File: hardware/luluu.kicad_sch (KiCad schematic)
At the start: 56 parts, among them J1 BATT_CON, J2 RPi SWD, J3 STEMMA_{QT} I_{2}C, J4 Micro_SD_Card, J5 RPi UART, J6 USB_C_Receptacle_USB2.0, J7 DISP_LCD_ST7789, Q1 AO3401A, Q2 BSS138, SW1 SW_USBBOOT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

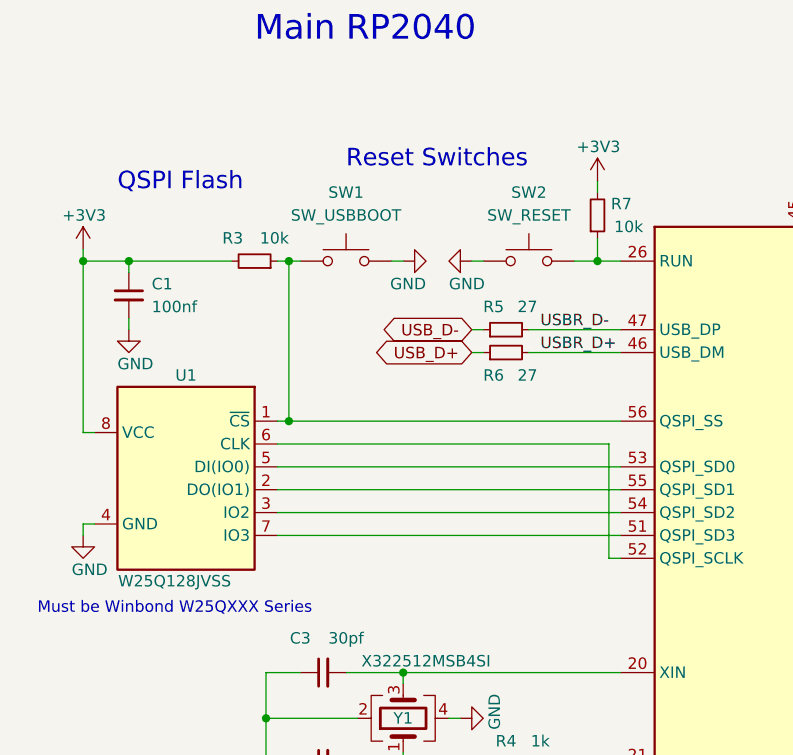
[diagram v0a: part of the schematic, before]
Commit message: rev1.1 - fix USB data and 1k boot resistor
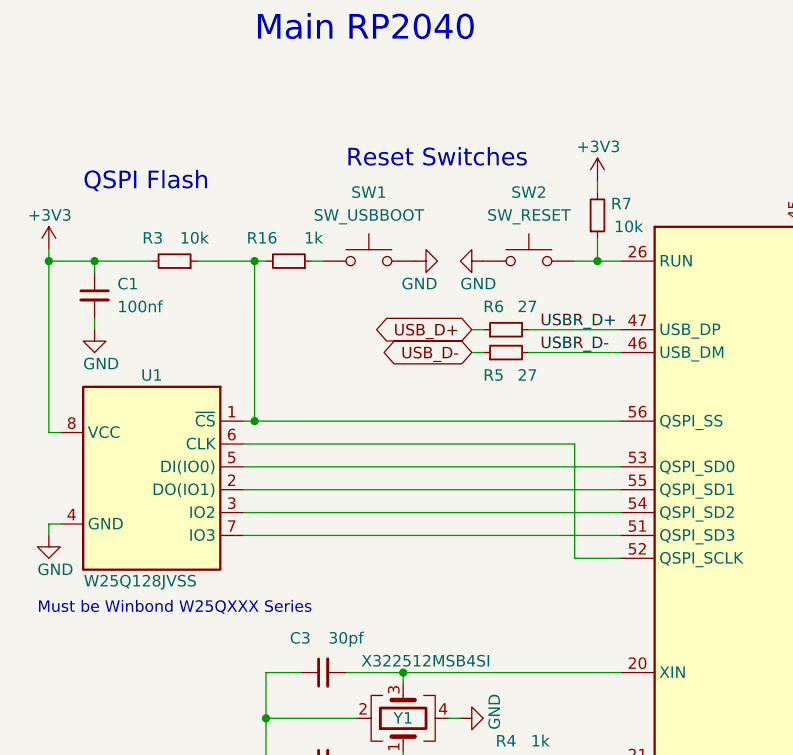
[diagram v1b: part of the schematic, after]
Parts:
- added R16: 1k, Resistor_SMD:R_0603_1608Metric_Pad0.98x0.95mm_HandSolder, symbol Device:R_Small
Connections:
- net USBR_D+: now also U3.47 (USB_DP); no longer U3.46 (USB_DM)
- net USBR_D-: now also U3.46 (USB_DM); no longer U3.47 (USB_DP)
- net at R3.1, U1.1 (~{CS}), U3.56 (QSPI_SS): now also R16.2; no longer SW1.1
- new net: R16.1, SW1.1
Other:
- moved on the sheet: C1, R3, R5, R6, SW1, U1

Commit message: start on rev2 of pcb
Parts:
- removed J5: RPi UART, Connector_JST:JST_SH_BM03B-SRSS-TB_1x03-1MP_P1.00mm_Vertical, symbol Connector_Generic:Conn_01x03
- removed U5: APX803S-26/29, Package_TO_SOT_SMD:SOT-23-3, symbol luluu:APX803S-26SA
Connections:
- net UART_{RX} is gone; now on net CARD_~{CS}: U3.3 (GPIO1)
- net +3V3: now also SW3.2 (B); no longer C5.1, C6.1, U2.5 (VOUT)
- net +BATT: now also J1.1 (Pin_1); no longer SW3.2 (B)
- net I_{2}C_{CLOCK}: now also U3.14 (GPIO11); no longer U3.5 (GPIO3)
- net I_{2}C_{DATA}: now also U3.13 (GPIO10); no longer U3.4 (GPIO2)
- net at SW3.1 (A): now also C5.1, C6.1, U2.5 (VOUT); no longer J1.1 (Pin_1)
- net CARD_SPI_{MISO}: now reaches U3.6 (GPIO4)
- net CARD_SPI_{MISO}: now also J4.7 (DAT0)
- net CARD ~{CS} renamed CARD_~{CS}
- net CARD_~{CS}: no longer U3.7 (GPIO5)
- net DISP BACKLIGHT renamed DISP_BACKLIGHT
- net DISP CS_{DATA/~{CMD}} renamed DISP_CS_{DATA/~{CMD}}
- net DISP VSYNC renamed DISP_VSYNC
- net DISP ~{CS_{MAIN}} renamed DISP_~{CS_{MAIN}}
- net DISP ~{RESET} renamed DISP_~{RESET}
- net SPI_{CLOCK} renamed DISP_SPI_{CLOCK}
- net DISP_SPI_{CLOCK}: no longer J4.5 (CLK)
- net SPI_{MISO}: no longer names the net of U3.11 (GPIO8)
- net SPI_{MISO}: no longer J4.7 (DAT0)
- net SPI_{MOSI} renamed DISP_SPI_{MOSI}
- net DISP_SPI_{MOSI}: no longer J4.3 (CMD)
- net UART_{TX}: no longer names the net of U3.2 (GPIO0)
- new net CARD_SPI_{CLOCK}: J4.5 (CLK), U3.4 (GPIO2)
- new net CARD_SPI_{MOSI}: J4.3 (CMD), U3.5 (GPIO3)
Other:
- note removed: "UART & I_{2}C compatible with Adafruit Feather GPIO Layout"
- moved on the sheet: J2, SW3

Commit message: pcb rev 2.0 progress
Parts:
- added D2: CHRG, LED_SMD:LED_0805_2012Metric_Pad1.15x1.40mm_HandSolder, symbol Device:LED
- added R17: 1k, Resistor_SMD:R_0603_1608Metric_Pad0.98x0.95mm_HandSolder, symbol Device:R_Small
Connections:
- net +5V: now also R17.2
- net CARD_SPI_{MISO}: now also U3.2 (GPIO0); no longer U3.6 (GPIO4)
- net CARD_~{CS}: now also U3.7 (GPIO5); no longer U3.3 (GPIO1)
- net at U4.1 (~{CHRG}): now also D2.1 (K)
- new net: D2.2 (A), R17.1
- no-connect marks 24 -> 23
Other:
- moved on the sheet: C7

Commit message: more work on v2.0
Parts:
- added J5: GPIO0, Connector_PinHeader_2.54mm:PinHeader_1x05_P2.54mm_Vertical, symbol Connector_Generic:Conn_01x05
- added J8: GPIO1, Connector_PinHeader_2.54mm:PinHeader_1x07_P2.54mm_Vertical, symbol Connector_Generic:Conn_01x07
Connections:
- net +3V3: now also J8.6 (Pin_6)
- net GND: now also J5.1 (Pin_1), J8.7 (Pin_7)
- net GPIO_D8: now reaches U3.11 (GPIO8)
- net GPIO_D8: now also J5.3 (Pin_3)
- net GPIO_D9: now reaches U3.12 (GPIO9)
- net GPIO_D9: now also J5.4 (Pin_4)
- net GPIO_D12: now reaches U3.15 (GPIO12)
- net GPIO_D12: now also J5.5 (Pin_5)
- net GPIO_D24: now reaches U3.36 (GPIO24)
- net GPIO_D24: now also J8.5 (Pin_5)
- net GPIO_D25: now reaches U3.37 (GPIO25)
- net GPIO_D25: now also J8.4 (Pin_4)
- net GPIO_A0: now reaches U3.38 (GPIO26_ADC0)
- net GPIO_A0: now also J8.3 (Pin_3)
- net GPIO_A1: now reaches U3.39 (GPIO27_ADC1)
- net GPIO_A1: now also J8.2 (Pin_2)
- net GPIO_A2: now reaches U3.40 (GPIO28_ADC2)
- net GPIO_A2: now also J8.1 (Pin_1)
- net GPIO_D7: now reaches U3.9 (GPIO7)
- net GPIO_D7: now also J5.2 (Pin_2)
- no-connect marks 23 -> 14

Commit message: more work on v2
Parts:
- added H1, H2, H3, H4, H5: MH, luluu:MountingHole_1.1mm_M1, symbol Mechanical:MountingHole
- added JP1: SW_A_JMPER, Jumper:SolderJumper-3_P1.3mm_Bridged12_RoundedPad1.0x1.5mm, symbol Jumper:SolderJumper_3_Bridged12
- added JP2: SW_B_JMPER, Jumper:SolderJumper-3_P1.3mm_Bridged12_RoundedPad1.0x1.5mm, symbol Jumper:SolderJumper_3_Bridged12
- SW1: value SW_USBBOOT -> SW_B
- SW2: value SW_RESET -> SW_A
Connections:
- net SW_A_RST: now reaches R7.1, U3.26 (RUN)
- net SW_A_RST: now also JP1.1 (A); no longer SW2.2
- net SW_A_GPIO: now reaches U3.3 (GPIO1)
- net SW_A_GPIO: now also JP1.3 (B)
- net SW_B_GPIO: now reaches U3.8 (GPIO6)
- net SW_B_GPIO: now also JP2.3 (B)
- net at SW1.1: now also JP2.2 (C); no longer R16.1
- new net: JP1.2 (C), SW2.2
- new net SW_B_BOOT: JP2.1 (A), R16.1
- no-connect marks 14 -> 12
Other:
- note added: "Mount Holes"
- note added: "Pin Headers"
- note added: "Push Switches"
- note removed: "Reset Switches"
- moved on the sheet: C1, C10, C11, C12, C13, C14, C15, C16, C17, C18, C19, C3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

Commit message: 2.0 release candidate
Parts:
- removed C21: 100nf, Capacitor_SMD:C_0402_1005Metric_Pad0.74x0.62mm_HandSolder, symbol Device:C_Small
- added C23: 100nf, Capacitor_SMD:C_0402_1005Metric_Pad0.74x0.62mm_HandSolder, symbol Device:C_Small
- added JP3: Accel Addr LSB, Jumper:SolderJumper-2_P1.3mm_Open_RoundedPad1.0x1.5mm, symbol Jumper:SolderJumper_2_Open
- added R18, R19: 5.1k, Resistor_SMD:R_0603_1608Metric_Pad0.98x0.95mm_HandSolder, symbol Device:R_Small
- added R20: 10k, Resistor_SMD:R_0603_1608Metric_Pad0.98x0.95mm_HandSolder, symbol Device:R_Small
- added U5: LIS3DH, Package_LGA:LGA-16_3x3mm_P0.5mm_LayoutBorder3x5y, symbol Sensor_Motion:LIS3DH
- H1, H2, H3: footprint luluu:MountingHole_1.1mm_M1 -> luluu:MountingHole_1.3mm_M1.2_Pad; now left out of the parts list
- H4, H5: footprint luluu:MountingHole_1.1mm_M1 -> luluu:MountingHole_1.3mm_M1.2; now left out of the parts list
- J5: footprint Connector_PinHeader_2.54mm:PinHeader_1x05_P2.54mm_Vertical -> luluu:PinHeader_1x06_P2.54mm_Vertical; symbol Connector_Generic:Conn_01x05 -> Connector_Generic:Conn_01x06; now left out of the parts list
- J7: footprint luluu:FPC_24_SOLDER -> luluu:FPC_24_JUSHUO_AFC04-S24XCA-00; LCSC (none) -> C883644; now in the parts list
- J8: footprint Connector_PinHeader_2.54mm:PinHeader_1x07_P2.54mm_Vertical -> luluu:PinHeader_1x07_P2.54mm_Vertical; now left out of the parts list
- JP1, JP2: now left out of the parts list
- R17: value 1k -> 10k
- R9: value 5.1k -> 10k
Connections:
- net +3V3: now also J8.7 (Pin_7), R3.1, R7.1, C23.1, JP3.1 (A), R18.1, R19.1, U5.1 (VDD_IO), U5.14 (VDD), U5.8 (CS); no longer J8.6 (Pin_6), R3.2, R7.2, R9.2
- net +BATT: now also J5.1 (Pin_1)
- net CARD_~{CS}: now also U3.6 (GPIO4); no longer U3.7 (GPIO5)
- net DISP_BACKLIGHT: now also R9.2, U3.13 (GPIO10); no longer R9.1, U3.34 (GPIO22)
- net DISP_CS_{DATA/~{CMD}}: now also U3.16 (GPIO13); no longer U3.29 (GPIO18)
- net DISP_~{CS_{MAIN}}: now also U3.15 (GPIO12); no longer U3.30 (GPIO19)
- net DISP_~{RESET}: now also U3.14 (GPIO11); no longer U3.28 (GPIO17)
- net GND: now also J5.2 (Pin_2), J8.6 (Pin_6), R9.1, C23.2, R20.1, U5.10 (GND), U5.12 (GND), U5.13 (ADC3), U5.15 (ADC2), U5.16 (ADC1), U5.5 (GND); no longer J5.1 (Pin_1), J8.7 (Pin_7)
- net GPIO_D24: now also U5.11 (INT1)
- net GPIO_D7: now also J5.4 (Pin_4); no longer J5.2 (Pin_2)
- net GPIO_D8: now also J5.5 (Pin_5); no longer J5.3 (Pin_3)
- net GPIO_D9: now also J5.6 (Pin_6); no longer J5.4 (Pin_4)
- net I_{2}C_{CLOCK}: now also U3.30 (GPIO19), R19.2, U5.4 (SCL/SPC); no longer U3.14 (GPIO11)
- net I_{2}C_{DATA}: now also U3.29 (GPIO18), R18.2, U5.6 (SDA/SDI/SDO); no longer U3.13 (GPIO10)
- net SW_A_RST: now also R7.2; no longer R7.1
- net SW_B_GPIO: now also U3.7 (GPIO5); no longer U3.8 (GPIO6)
- net at R16.2, U1.1 (~{CS}), U3.56 (QSPI_SS): now also R3.2; no longer R3.1
- removed net GPIO_D12: J5.5 (Pin_5), U3.15 (GPIO12)
- new net: JP3.2 (B), R20.2, U5.7 (SDO/SA0)
- new net GPIO_D6: J5.3 (Pin_3), U3.8 (GPIO6)
- no-connect marks 12 -> 13
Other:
- note added: "Accelerometer"
- note added: "Connector specified by RPi Debug Connector Specification"
- note removed: "Connectors specified by RPi Debug Connector Specification"
- note removed: "RP2040 I/O Pins"
- moved on the sheet: C10, C11, C8, C9, D2, H4, H5, J1, J2, J3, J8, JP1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
